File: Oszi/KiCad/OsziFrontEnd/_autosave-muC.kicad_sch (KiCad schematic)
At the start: 1 part, among them U3 NUCLEO-L432KC

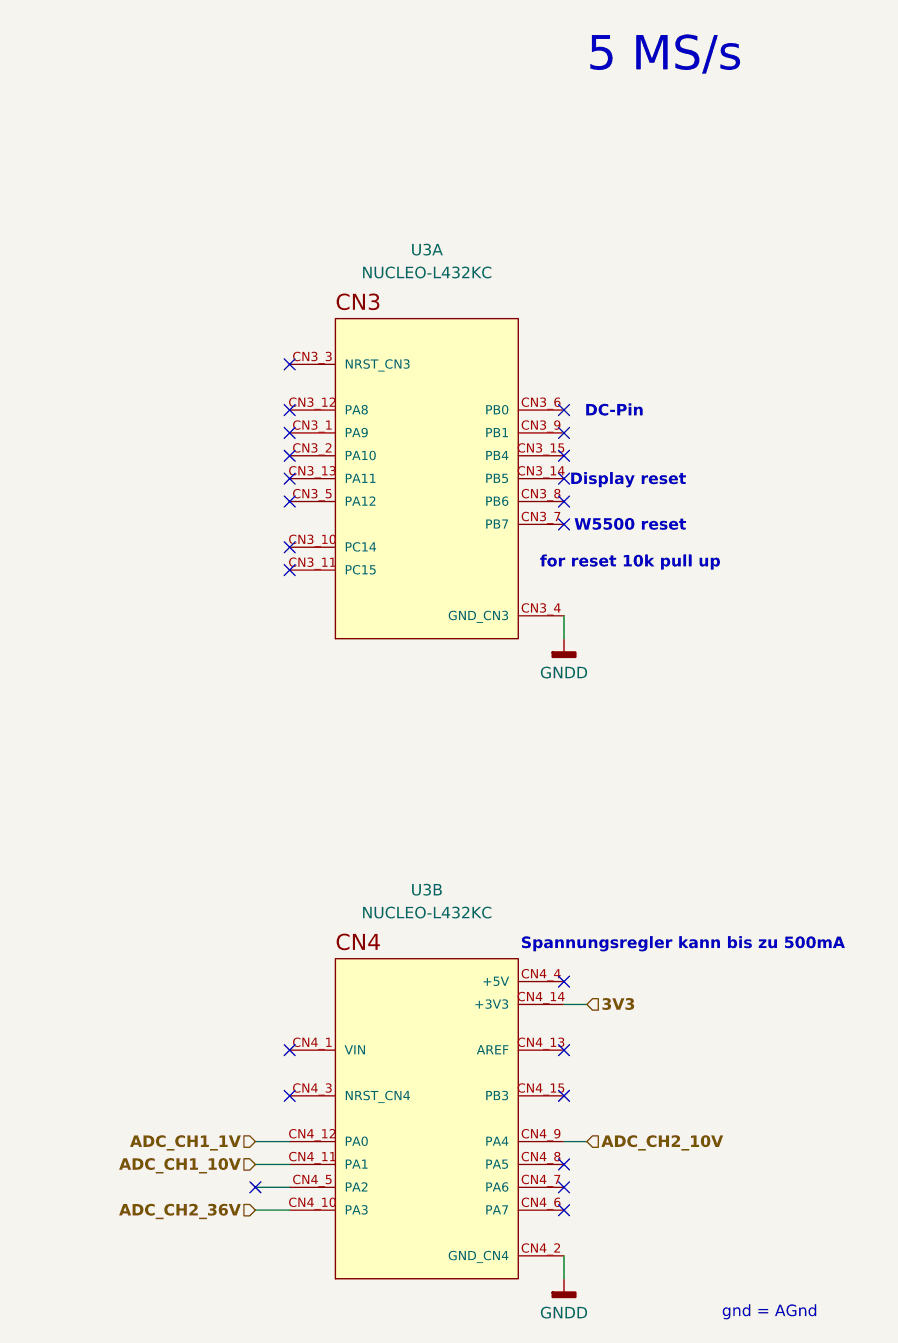
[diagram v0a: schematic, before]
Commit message: added display in KiCad
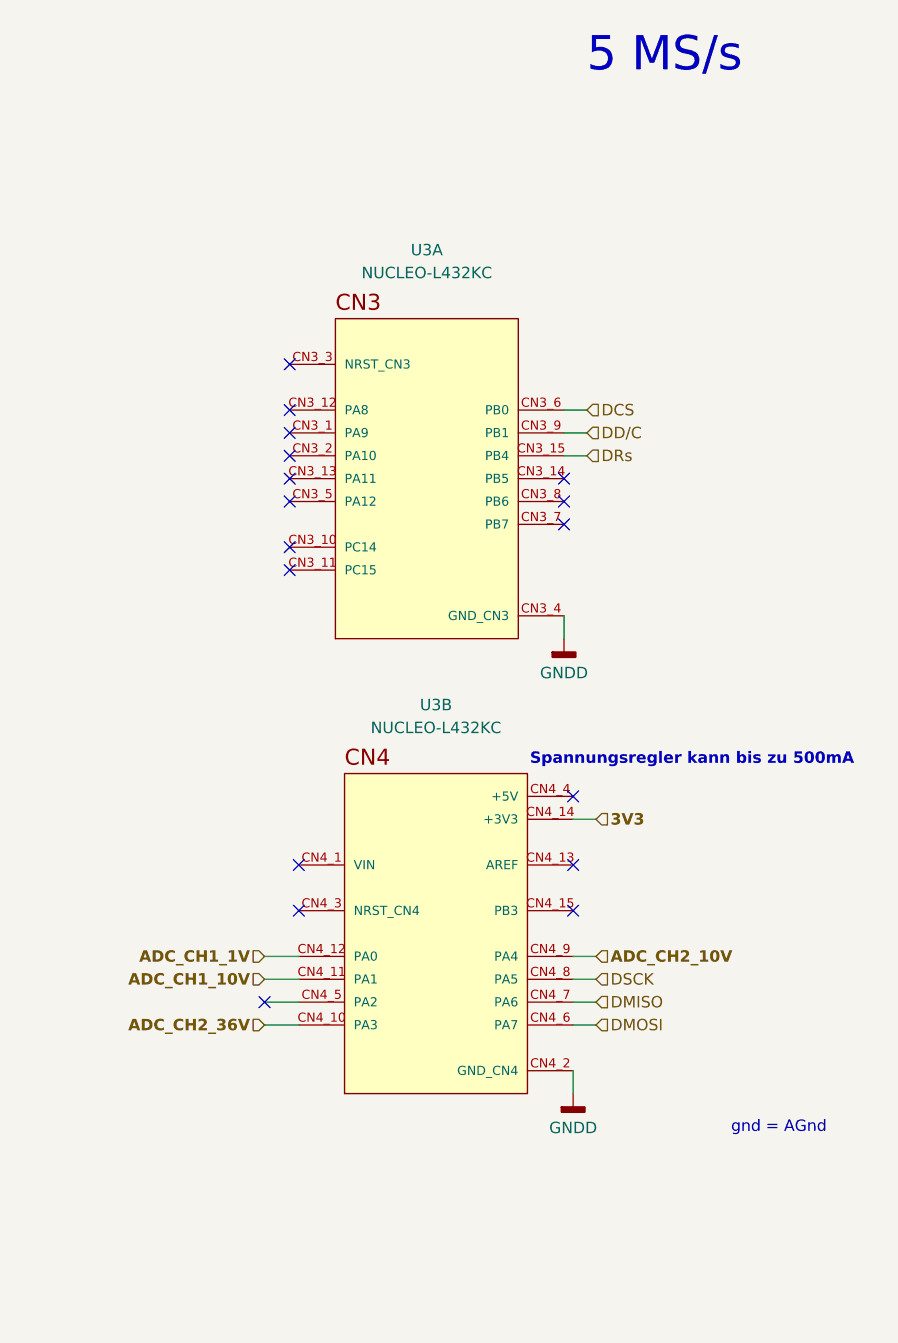
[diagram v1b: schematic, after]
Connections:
- net DMOSI: now reaches U3.CN4_6 (PA7)
- net DMISO: now reaches U3.CN4_7 (PA6)
- net DSCK: now reaches U3.CN4_8 (PA5)
- net DRs: now reaches U3.CN3_15 (PB4)
- net DCS: now reaches U3.CN3_6 (PB0)
- net DD/C: now reaches U3.CN3_9 (PB1)
- no-connect marks 23 -> 17
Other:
- note removed: "DC-Pin"
- note removed: "Display reset"
- note removed: "W5500 reset for reset 10k pull up"
- moved on the sheet: U3B

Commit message: added buttons 4 display
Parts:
- added RV1: R_Potentiometer, symbol Device:R_Potentiometer
- added SW1, SW2, SW3: SW_Push, Button_Switch_SMD:SW_SPST_PTS645Sx43SMTR92, symbol Switch:SW_Push
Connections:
- net 3V3: now also SW1.1, SW2.1, SW3.2
- net EINT: now reaches U3.CN3_12 (PA8)
- net at U3.CN3_13 (PA11): now also SW2.2
- net at U3.CN3_14 (PB5): now also SW3.1
- net at U3.CN3_2 (PA10): now also SW1.2
- net ERs: now reaches U3.CN3_7 (PB7)
- net ECS: now reaches U3.CN3_8 (PB6)
- net DMISO renamed MISO
- net DMOSI renamed MOSI
- net DSCK renamed SCK
- no-connect marks 17 -> 10
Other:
- note added: "PB7, 6, PA8"
